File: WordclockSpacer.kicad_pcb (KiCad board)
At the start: 2 copper layers, 320.5 x 91 mm, 146 parts, among them J1 Input, J10 LED1, J11 LED7, J12 LED2Back, J13 LED2, J14 LED5, J15 LED8, J16 LED6, J17 Conn_01x03_Female, J18 LED1, J19 LED7, J2 Conn_01x02_Male, J20 LED2, J21 LED5, J22 LED8, J23 LED6, J24 LED9, J25 LED1, J26 LED7, J27 LED2, J28 LED5, J29 LED8, J3 Conn_01x02_Male, J30 LED6, J31 LED9, J32 Conn_01x10, J33 Conn_01x10, J34 LED4, J35 LED4, J36 Conn_02x04_Odd_Even, J37 Conn_01x03_Female, J38 LED_OUT, J39 LED_IN, J4 Output, J40 LED_IN, J5 Middle Out, J6 Back Line In, J7 Back Line Out middle, J8 Back Line Out, J9 LED1Back, SW1 SW_Push, U1 ESP-12E, U2 74HCT1G125GW

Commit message: improved footprint
Signed-off-by: Empire
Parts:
- removed REF** (x12): MountingHole_3.2mm_M3, MountingHole:MountingHole_3.2mm_M3
- removed REF**: MountingHole_2.5mm, MountingHole:MountingHole_2.5mm
- D1, D10, D11, D12, D13, D14, D15, D16, D17, D18, D19, D2, D20, D21, D22, D23, D24, D25, D26, D27, D28, D29, D3, D30, D31, D32, D33, D34, D35, D36, D37, D38, D39, D4, D40, D5, D6, D7, D8, D9: footprint LED_SMD:LED_WS2812B_PLCC4_5.0x5.0mm_P3.2mm -> Wordclock:LED_WS2812B_PLCC4_5.0x5.0mm_P3.2mmMitEcke
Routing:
- net +5V: track 2088.5 -> 2104.8 mm
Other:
- board text added: "LED baseboard v2.4"
- board text removed: "LED baseboard v2.3"

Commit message: GPIO Names fixed
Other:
- board text added: "GPIO 0 GPIO 1 / TXD GPIO 2 GPIO 3 / RXD GPIO 5 GPIO 4 GPIO 12 GPIO 13 GPIO 14 GPIO 15"
- board text removed: "GPIO 0 GPIO 1 / TXD GPIO 2 GPIO 3 / RXD GPIO 5 GPIO 4 GPIO 12 GPIO 13 GPIO 14 GPIO 15 GPIO 16"
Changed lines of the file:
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@@
     (effects (font (size 1.5 1.5) (thickness 0.3)) (justify right mirror))
   )
-  (gr_text "GPIO 0\nGPIO 1 / TXD\nGPIO 2\nGPIO 3 / RXD\nGPIO 5\nGPIO 4\nGPIO 12\nGPIO 13\nGPIO 14\nGPIO 15\nGPIO 16" (at 89.4 107.6 90) (layer B.SilkS)
-    (effects (font (size 1.3 1.3) (thickness 0.3)) (justify left mirror))
+  (gr_text "GPIO 0\nGPIO 1 / TXD\nGPIO 2\nGPIO 3 / RXD\nGPIO 5\nGPIO 4\nGPIO 12\nGPIO 13\nGPIO 14\nGPIO 15" (at 89.4 107.6 90) (layer B.SilkS)
+    (effects (font (size 1.45 1.45) (thickness 0.3)) (justify left mirror))
   )
   (gr_text "Line 3" (at 146 109.8) (layer F.SilkS)

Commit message: V3 Alpha
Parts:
- added J41: Conn_02x20_Odd_Even, Connector_PinSocket_2.54mm:PinSocket_2x20_P2.54mm_Vertical, F.Cu at (121.6, 67.9)
- added J42: Conn_02x20_Counter_Clockwise, Connector_PinSocket_2.54mm:PinSocket_2x20_P2.54mm_Vertical, F.Cu at (121.6, 73.4)
- added J43: Conn_02x20_Counter_Clockwise, Connector_PinSocket_2.54mm:PinSocket_2x20_P2.54mm_Vertical, F.Cu at (210.3, 73.0)
- added J44: Conn_02x20_Odd_Even, Connector_PinSocket_2.54mm:PinSocket_2x20_P2.54mm_Vertical, F.Cu at (210.2, 67.6)
- added REF**: MountingHole_2.7mm_M2.5, MountingHole:MountingHole_2.7mm_M2.5, F.Cu at (346.8, 57.0)
- added REF**: MountingHole_2.7mm_M2.5, MountingHole:MountingHole_2.7mm_M2.5, F.Cu at (118.0, 55.8)
- added REF**: MountingHole_2.7mm_M2.5, MountingHole:MountingHole_2.7mm_M2.5, F.Cu at (62.8, 55.8)
- added REF**: MountingHole_2.7mm_M2.5, MountingHole:MountingHole_2.7mm_M2.5, F.Cu at (62.2, 117.8)
- added REF**: MountingHole_2.7mm_M2.5, MountingHole:MountingHole_2.7mm_M2.5, F.Cu at (174.0, 117.4)
- added REF**: MountingHole_2.7mm_M2.5, MountingHole:MountingHole_2.7mm_M2.5, F.Cu at (346.8, 114.6)
- added REF**: MountingHole_2.7mm_M2.5, MountingHole:MountingHole_2.7mm_M2.5, F.Cu at (314.0, 126.4)
- added REF**: MountingHole_2.7mm_M2.5, MountingHole:MountingHole_2.7mm_M2.5, F.Cu at (230.0, 117.2)
- added REF**: MountingHole_2.7mm_M2.5, MountingHole:MountingHole_2.7mm_M2.5, F.Cu at (285.6, 117.2)
- added REF**: MountingHole_2.7mm_M2.5, MountingHole:MountingHole_2.7mm_M2.5, F.Cu at (313.4, 46.8)
- added REF**: MountingHole_2.7mm_M2.5, MountingHole:MountingHole_2.7mm_M2.5, F.Cu at (285.6, 55.8)
- added REF**: MountingHole_2.7mm_M2.5, MountingHole:MountingHole_2.7mm_M2.5, F.Cu at (230.0, 56.0)
- added REF**: MountingHole_2.7mm_M2.5, MountingHole:MountingHole_2.7mm_M2.5, F.Cu at (173.8, 56.0)
- C1, C10, C11, C12, C15, C16, C17, C18, C19, C2, C20, C21, C22, C23, C24, C25, C26, C27, C28, C29, C3, C30, C31, C32, C33, C34, C35, C36, C37, C38, C39, C4, C40, C41, C42, C45, C5, C6, C7, C8, C9: footprint Capacitor_SMD:C_1206_3216Metric -> Capacitor_SMD:C_0805_2012Metric_Pad1.15x1.40mm_HandSolder
- J1: footprint Connector_PinSocket_2.54mm:PinSocket_1x07_P2.54mm_Horizontal -> Connector_PinHeader_2.54mm:PinHeader_1x07_P2.54mm_Vertical
- J17: footprint Connector_PinSocket_2.54mm:PinSocket_1x03_P2.54mm_Vertical -> Connector_PinSocket_2.54mm:PinSocket_1x03_P2.54mm_Horizontal
- J36: footprint Connector_PinHeader_2.54mm:PinHeader_2x04_P2.54mm_Vertical -> Connector_PinSocket_2.54mm:PinSocket_2x04_P2.54mm_Vertical
- J38, J39, J40: footprint Connector_PinHeader_2.54mm:PinHeader_1x01_P2.54mm_Vertical -> Connector_PinSocket_2.54mm:PinSocket_1x01_P2.54mm_Horizontal
- J4, J5: footprint Connector_PinHeader_2.54mm:PinHeader_1x07_P2.54mm_Horizontal -> Connector_PinSocket_2.54mm:PinSocket_1x07_P2.54mm_Horizontal
- J7, J8: footprint Connector_PinHeader_2.54mm:PinHeader_1x03_P2.54mm_Horizontal -> Connector_PinSocket_2.54mm:PinSocket_1x03_P2.54mm_Horizontal
- R1, R2, R3, R4, R5: footprint Resistor_SMD:R_0805_2012Metric -> Resistor_SMD:R_0805_2012Metric_Pad1.15x1.40mm_HandSolder
- U2: footprint SOT65P210X110-5N -> 74HCT1G125GW:SOT65P210X110-5N
- moved C43 34.0 mm to (199.9, 99.8), turned to 0 degrees
- moved C40 3.74 mm to (55.4, 60.0)
- moved J36 2.60 mm to (117.0, 105.4)
- moved C29 1.92 mm to (243.6, 79.0)
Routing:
- net GND: track 86.8 -> 643.4 mm, vias 159 -> 143
- net +3V3: track 156.2 -> 243.4 mm
- net +5V: track 2104.8 -> 2189.2 mm, vias 21 -> 23
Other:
- board text added: "5.0V EMV Free GND (EMV!)"
- board text added: "LED baseboard v3.0 Alpha RTM"
- board text removed: "LED baseboard v2.4"

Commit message: no Alpha. it is V3
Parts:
- moved C43 18.2 mm to (200.0, 118.0)
- moved C30 2.45 mm to (77.6, 77.2)
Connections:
- J32 pad 7: Net-(J32-Pad7) -> GND
- R3 pad 2: Net-(J33-Pad10) -> Net-(J33-Pad7)
- U1 pad 1: Net-(J32-Pad10) -> Net-(J32-Pad3)
- U1 pad 10: Net-(J32-Pad6) -> Net-(J32-Pad8)
- U1 pad 11: Net-(J32-Pad5) -> Net-(J32-Pad2)
- U1 pad 12: Net-(J32-Pad4) -> Net-(J32-Pad1)
- U1 pad 13: Net-(J32-Pad3) -> Net-(J33-Pad10)
- U1 pad 14: Net-(J32-Pad2) -> Net-(J33-Pad9)
- U1 pad 16: Net-(J33-Pad10) -> Net-(J33-Pad7)
- U1 pad 2: Net-(J32-Pad8) -> Net-(J32-Pad4)
- U1 pad 4: Net-(J32-Pad1) -> Net-(J32-Pad5)
- U1 pad 5: Net-(J33-Pad9) -> Net-(J32-Pad6)
- U1 pad 6: Net-(J33-Pad7) -> GND
- U1 pad 9: Net-(J32-Pad7) -> Net-(J32-Pad10)
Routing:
- net Net-(J33-Pad9): track 77.6 -> 13.4 mm
- net Net-(J32-Pad3): track 67.8 -> 7.57 mm
- net Net-(J33-Pad7): track 67.6 -> 10.7 mm
- net Net-(J32-Pad4): track 56.6 -> 7.45 mm
- net Net-(J32-Pad1): track 17.7 -> 63.3 mm
- net +5V: track 2189.2 -> 2149.5 mm
- net Net-(J32-Pad5): track 47.2 -> 7.96 mm
- net Net-(J32-Pad6): track 34.9 -> 7.73 mm
- net Net-(J32-Pad2): track 77.2 -> 53.5 mm
- net Net-(J32-Pad7): track 17.9 -> 0.00 mm, vias 2 -> 0
- net GND: track 643.4 -> 660.1 mm, vias 143 -> 181
- net Net-(J32-Pad10): track 23.6 -> 11.1 mm, vias 2 -> 0
- net Net-(J32-Pad8): track 17.7 -> 29.8 mm, vias 2 -> 0
- net +3V3: track 243.4 -> 232.9 mm, vias 2 -> 1
- net Net-(J33-Pad10): track 12.7 -> 16.3 mm
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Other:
- board text added: "GPIO 0 GPIO 1 / TXD GPIO 2 GPIO 3 / RXD GPIO 5 GPIO 4 GPIO 15 GPIO13 SCLK MOSI"
- board text added: "GPIO10 GPIO9 NOT RST ADC GPIO16 GPIO14 GPIO12 MISO 3V3 CS"
- board text added: "LED baseboard v3.0"
- board text removed: "GPIO 0 GPIO 1 / TXD GPIO 2 GPIO 3 / RXD GPIO 5 GPIO 4 GPIO 12 GPIO 13 GPIO 14 GPIO 15"
- board text removed: "LED baseboard v3.0 Alpha RTM"
- board text removed: "SLCK MOSI GPIO10 GPIO9 MOSI CSO ADC EN 3.3 V NOT RST"

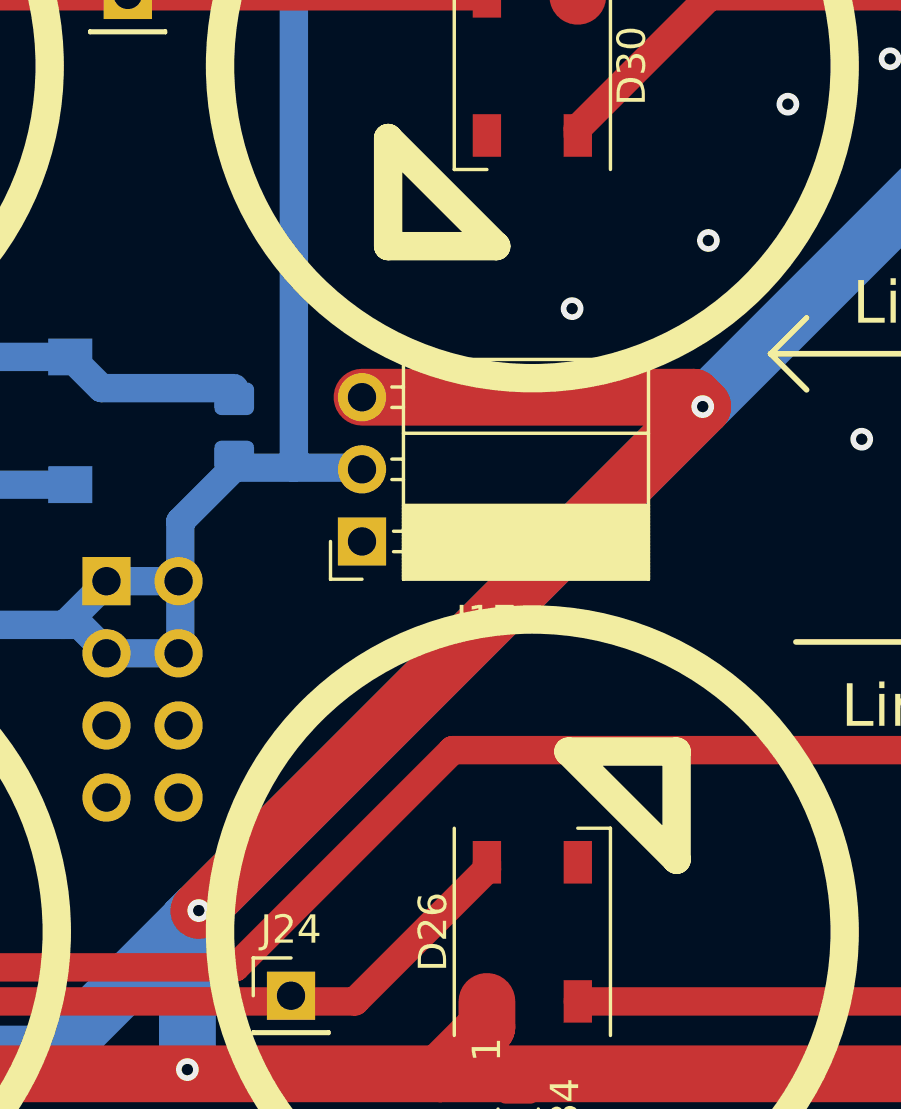
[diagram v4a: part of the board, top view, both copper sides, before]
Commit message: V3.0 added AMS1117
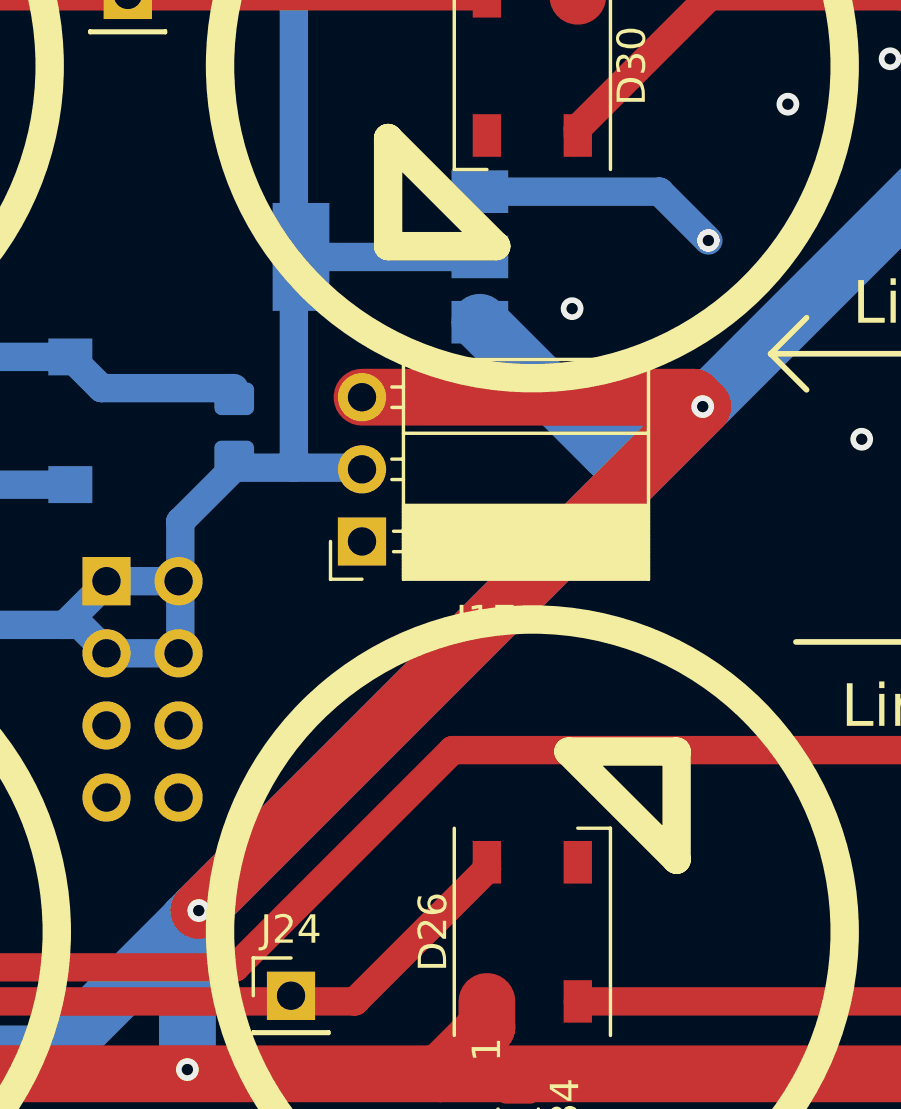
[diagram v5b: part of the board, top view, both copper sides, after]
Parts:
- added U3: AMS1117-3.3, Package_TO_SOT_SMD:SOT-223-3_TabPin2, B.Cu at (127.0, 94.0)
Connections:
- J42 pad 1: (no net) -> unconnected-(J42-Pad1)
- J42 pad 10: (no net) -> unconnected-(J42-Pad10)
- J42 pad 11: (no net) -> unconnected-(J42-Pad11)
- J42 pad 12: (no net) -> unconnected-(J42-Pad12)
- J42 pad 13: (no net) -> unconnected-(J42-Pad13)
- J42 pad 14: (no net) -> unconnected-(J42-Pad14)
- J42 pad 15: (no net) -> unconnected-(J42-Pad15)
- J42 pad 16: (no net) -> unconnected-(J42-Pad16)
- J42 pad 17: (no net) -> unconnected-(J42-Pad17)
- J42 pad 18: (no net) -> unconnected-(J42-Pad18)
- J42 pad 19: (no net) -> unconnected-(J42-Pad19)
- J42 pad 2: (no net) -> unconnected-(J42-Pad2)
- J42 pad 20: (no net) -> unconnected-(J42-Pad20)
- J42 pad 21: (no net) -> unconnected-(J42-Pad21)
- J42 pad 22: (no net) -> unconnected-(J42-Pad22)
- J42 pad 23: (no net) -> unconnected-(J42-Pad23)
- J42 pad 24: (no net) -> unconnected-(J42-Pad24)
- J42 pad 25: (no net) -> unconnected-(J42-Pad25)
- J42 pad 26: (no net) -> unconnected-(J42-Pad26)
- J42 pad 27: (no net) -> unconnected-(J42-Pad27)
- J42 pad 28: (no net) -> unconnected-(J42-Pad28)
- J42 pad 29: (no net) -> unconnected-(J42-Pad29)
- J42 pad 3: (no net) -> unconnected-(J42-Pad3)
- J42 pad 30: (no net) -> unconnected-(J42-Pad30)
- J42 pad 31: (no net) -> unconnected-(J42-Pad31)
- J42 pad 32: (no net) -> unconnected-(J42-Pad32)
- J42 pad 33: (no net) -> unconnected-(J42-Pad33)
- J42 pad 34: (no net) -> unconnected-(J42-Pad34)
- J42 pad 35: (no net) -> unconnected-(J42-Pad35)
- J42 pad 36: (no net) -> unconnected-(J42-Pad36)
- J42 pad 37: (no net) -> unconnected-(J42-Pad37)
- J42 pad 38: (no net) -> unconnected-(J42-Pad38)
- J42 pad 39: (no net) -> unconnected-(J42-Pad39)
- J42 pad 4: (no net) -> unconnected-(J42-Pad4)
- J42 pad 40: (no net) -> unconnected-(J42-Pad40)
- J42 pad 5: (no net) -> unconnected-(J42-Pad5)
- J42 pad 6: (no net) -> unconnected-(J42-Pad6)
- J42 pad 7: (no net) -> unconnected-(J42-Pad7)
- J42 pad 8: (no net) -> unconnected-(J42-Pad8)
- J42 pad 9: (no net) -> unconnected-(J42-Pad9)
- J43 pad 1: (no net) -> unconnected-(J43-Pad1)
- J43 pad 10: (no net) -> unconnected-(J43-Pad10)
- J43 pad 11: (no net) -> unconnected-(J43-Pad11)
- J43 pad 12: (no net) -> unconnected-(J43-Pad12)
- J43 pad 13: (no net) -> unconnected-(J43-Pad13)
- J43 pad 14: (no net) -> unconnected-(J43-Pad14)
- J43 pad 15: (no net) -> unconnected-(J43-Pad15)
- J43 pad 16: (no net) -> unconnected-(J43-Pad16)
- J43 pad 17: (no net) -> unconnected-(J43-Pad17)
- J43 pad 18: (no net) -> unconnected-(J43-Pad18)
- J43 pad 19: (no net) -> unconnected-(J43-Pad19)
- J43 pad 2: (no net) -> unconnected-(J43-Pad2)
- J43 pad 20: (no net) -> unconnected-(J43-Pad20)
- J43 pad 21: (no net) -> unconnected-(J43-Pad21)
- J43 pad 22: (no net) -> unconnected-(J43-Pad22)
- J43 pad 23: (no net) -> unconnected-(J43-Pad23)
- J43 pad 24: (no net) -> unconnected-(J43-Pad24)
- J43 pad 25: (no net) -> unconnected-(J43-Pad25)
- J43 pad 26: (no net) -> unconnected-(J43-Pad26)
- J43 pad 27: (no net) -> unconnected-(J43-Pad27)
- J43 pad 28: (no net) -> unconnected-(J43-Pad28)
- J43 pad 29: (no net) -> unconnected-(J43-Pad29)
- J43 pad 3: (no net) -> unconnected-(J43-Pad3)
- J43 pad 30: (no net) -> unconnected-(J43-Pad30)
- J43 pad 31: (no net) -> unconnected-(J43-Pad31)
- J43 pad 32: (no net) -> unconnected-(J43-Pad32)
- J43 pad 33: (no net) -> unconnected-(J43-Pad33)
- J43 pad 34: (no net) -> unconnected-(J43-Pad34)
- J43 pad 35: (no net) -> unconnected-(J43-Pad35)
- J43 pad 36: (no net) -> unconnected-(J43-Pad36)
- J43 pad 37: (no net) -> unconnected-(J43-Pad37)
- J43 pad 38: (no net) -> unconnected-(J43-Pad38)
- J43 pad 39: (no net) -> unconnected-(J43-Pad39)
- J43 pad 4: (no net) -> unconnected-(J43-Pad4)
- J43 pad 40: (no net) -> unconnected-(J43-Pad40)
- J43 pad 5: (no net) -> unconnected-(J43-Pad5)
- J43 pad 6: (no net) -> unconnected-(J43-Pad6)
- J43 pad 7: (no net) -> unconnected-(J43-Pad7)
- J43 pad 8: (no net) -> unconnected-(J43-Pad8)
- J43 pad 9: (no net) -> unconnected-(J43-Pad9)
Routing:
- net GND: track 660.1 -> 668.8 mm
- net +5V: track 2149.5 -> 2157.6 mm
- net +3V3: track 232.9 -> 239.2 mm
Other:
- net class Default removed
- net class Enny removed
- net class Power removed
